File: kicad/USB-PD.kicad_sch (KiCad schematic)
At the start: 23 parts

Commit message: Adding seperate USB-PD project
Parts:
- C14, C15, C23, C24, C25, C4, C5, C7, C8, C9, D2, R11, R15, R24, R28, R29, R30, R37, R39, R40, R42, R43: value (none) -> ~

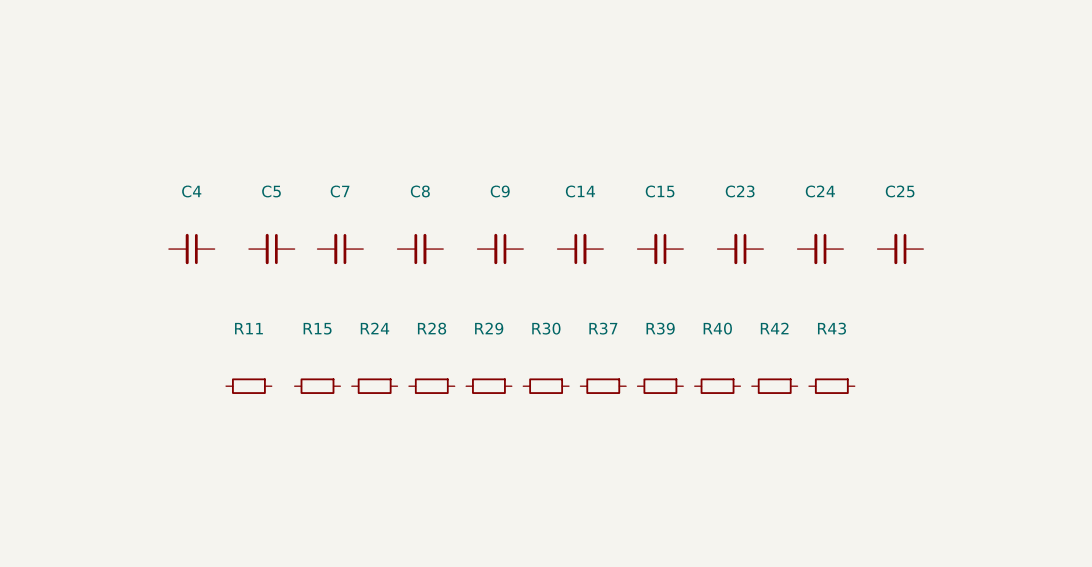
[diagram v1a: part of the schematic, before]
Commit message: Some overwritten changes by swapping back to robot project
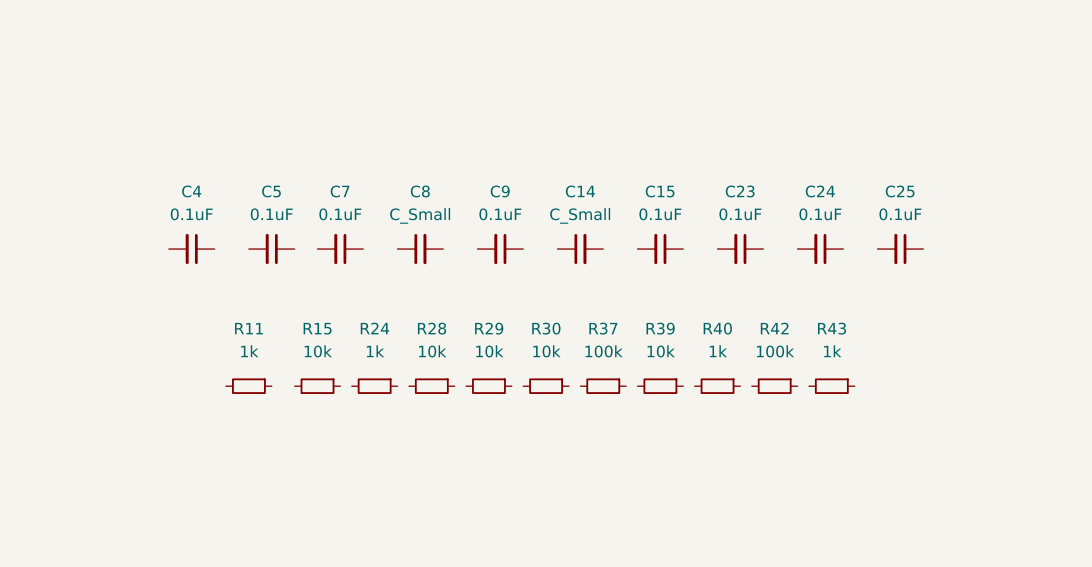
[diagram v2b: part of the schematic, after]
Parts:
- C14, C8: value ~ -> C_Small; footprint (none) -> Capacitor_SMD:C_0603_1608Metric
- C15, C23, C24, C25, C4, C5, C7, C9: value ~ -> 0.1uF; footprint (none) -> Capacitor_SMD:C_0402_1005Metric
- R11, R24, R40, R43: value ~ -> 1k; footprint (none) -> Resistor_SMD:R_0603_1608Metric
- R15, R28, R29, R30, R39: value ~ -> 10k; footprint (none) -> Resistor_SMD:R_0603_1608Metric
- R37, R42: value ~ -> 100k; footprint (none) -> Resistor_SMD:R_0402_1005Metric
